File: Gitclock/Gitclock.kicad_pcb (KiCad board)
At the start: 2 copper layers, 140 x 90 mm, 41 parts, among them J1 PJ-102AH, J2 Conn_01x06, SW1 Omron_B3F_SPST, SW5 RotaryEncoder_Switch, U1 ATmega328-PU, U2 L7805, U3 MAX7219, U4 DS1307_DIP-8, Y1 Crystal_16MHz, Y2 Crystal_32768Hz

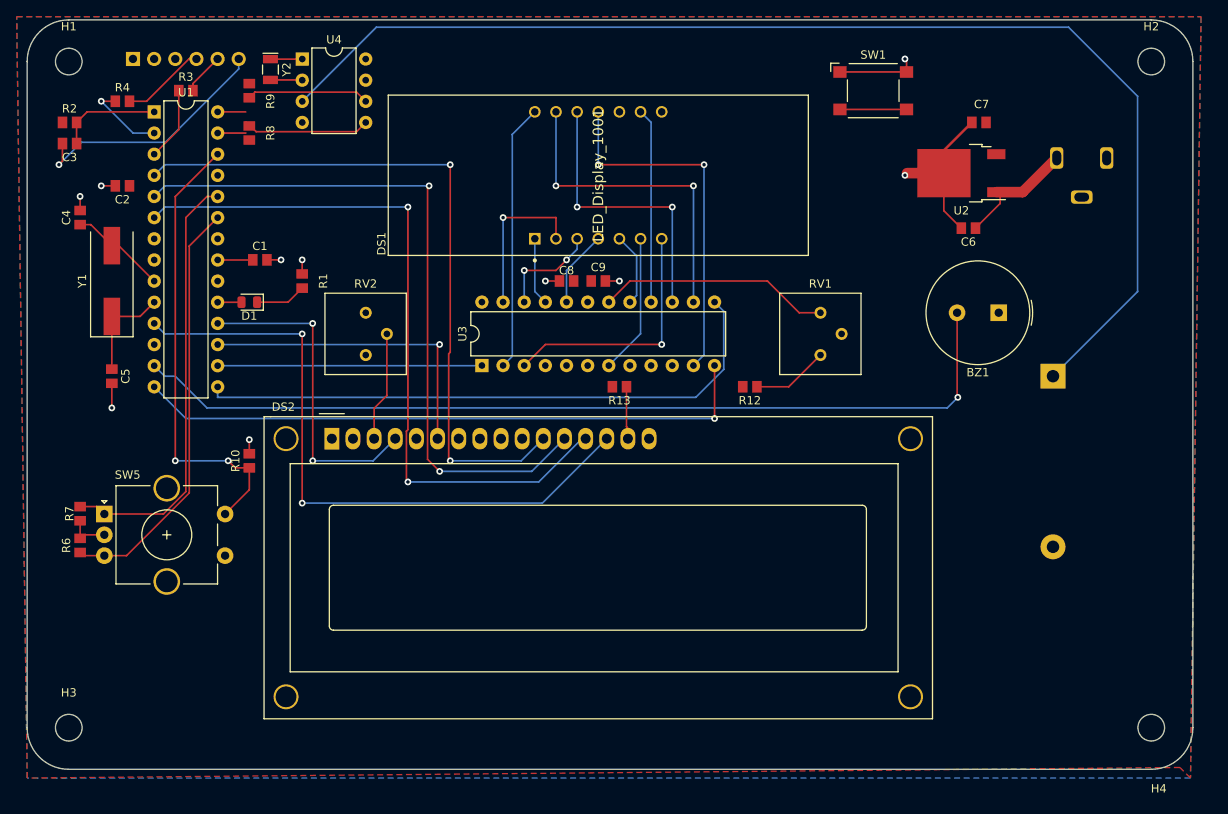
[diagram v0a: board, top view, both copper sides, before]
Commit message: Finished Routing each individual connections
Waiting for approval
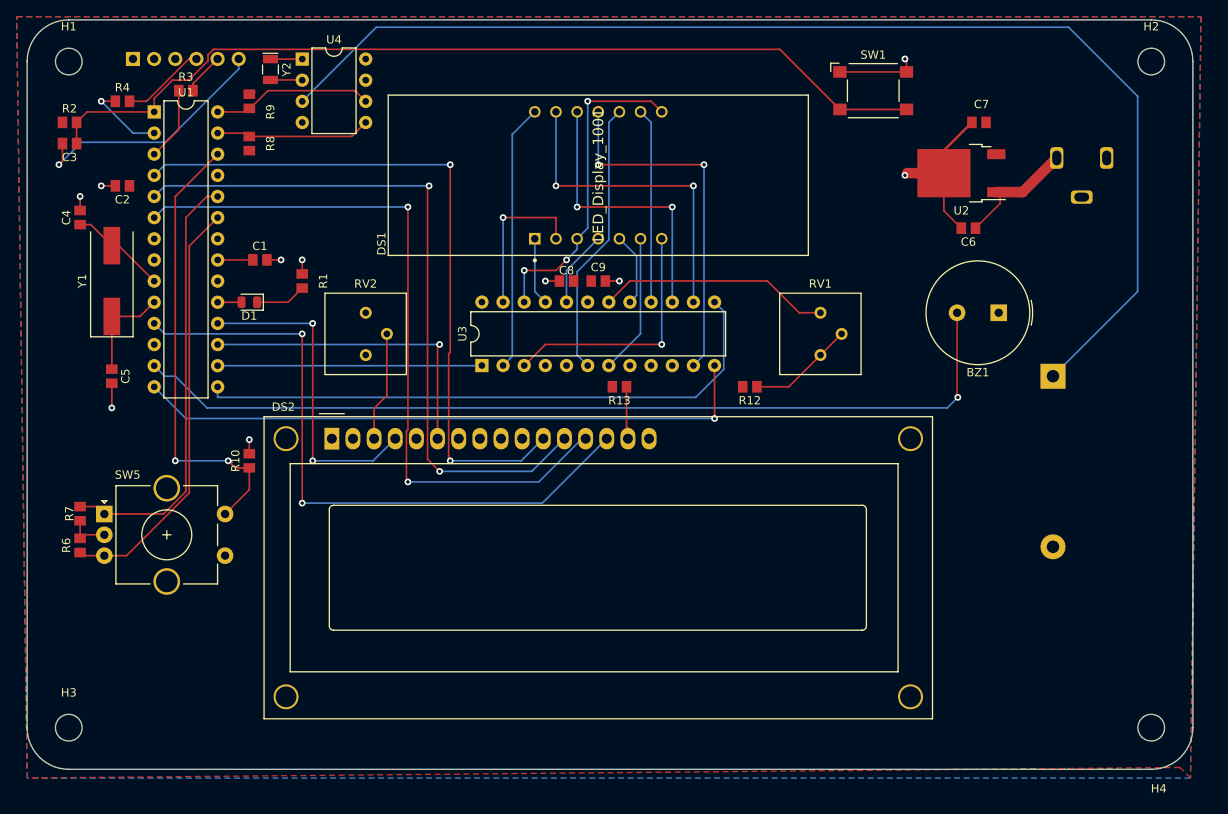
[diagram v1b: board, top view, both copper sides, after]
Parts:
- moved R8 1.27 mm to (106.7, 69.8)
- moved R9 1.27 mm to (106.7, 64.8)
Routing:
- net RESET: track 20.4 -> 110.2 mm
- net Net-(DS1-Pad10): track 0.00 -> 33.1 mm
- net Net-(DS1-Pad3): track 12.5 -> 38.9 mm, vias 2 -> 3
- net Net-(R12-Pad1): track 9.21 -> 12.8 mm
- net VCC: track 1.01 -> 1.96 mm
- net SCL: track 18.7 -> 19.4 mm
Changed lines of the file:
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@@
     (fp_line (start -5 28) (end -5 3) (layer "F.SilkS") (width 0.12))
     (fp_line (start -8.14 33.64) (end 72.14 33.64) (layer "F.SilkS") (width 0.12))
-    (fp_arc (start 64.20104 22.49932) (mid 64.054473 22.853115) (end 63.70066 22.9997) (layer "F.SilkS") (width 0.12))
+    (fp_arc (start 64.20104 22.49932) (mid 64.054479 22.85315) (end 63.70066 22.9997) (layer "F.SilkS") (width 0.12))
     (fp_arc (start -0.29972 8.49884) (mid -0.153162 8.145018) (end 0.20066 7.99846) (layer "F.SilkS") (width 0.12))
     (fp_arc (start 0.20066 22.9997) (mid -0.153162 22.853142) (end -0.29972 22.49932) (layer "F.SilkS") (width 0.12))
@@
   )
   (footprint "footprints:R_0805_2012Metric" (layer "F.Cu")
-    (at 106.68 63.5 -90)
+    (at 106.68 64.77 -90)
     (descr "Resistor SMD 0805 (2012 Metric), square (rectangular) end terminal, IPC_7351 nominal, (Body size source: http://www.tortai-tech.com/upload/download/2011102023233369053.pdf), generated with kicad-footprint-generator")
     (tags "resistor")
@@
   )
   (footprint "footprints:R_0805_2012Metric" (layer "F.Cu")
-    (at 106.68 68.58 90)
+    (at 106.68 69.85 90)
     (descr "Resistor SMD 0805 (2012 Metric), square (rectangular) end terminal, IPC_7351 nominal, (Body size source: http://www.tortai-tech.com/upload/download/2011102023233369053.pdf), generated with kicad-footprint-generator")
     (tags "resistor")
@@
   (segment (start 107.09 83.83) (end 107.1 83.82) (width 0.2032) (layer "F.Cu") (net 2))
   (segment (start 102.88 83.83) (end 107.09 83.83) (width 0.2032) (layer "F.Cu") (net 2))
+  (segment (start 97.456501 62.23) (end 95.26 64.426501) (width 0.2032) (layer "F.Cu") (net 3))
+  (segment (start 101.715689 59.936754) (end 99.422443 62.23) (width 0.2032) (layer "F.Cu") (net 3))
+  (segment (start 101.715689 59.211868) (end 101.715689 59.936754) (width 0.2032) (layer "F.Cu") (net 3))
+  (segment (start 99.422443 62.23) (end 97.456501 62.23) (width 0.2032) (layer "F.Cu") (net 3))
   (segment (start 87.2 66.05) (end 95.26 66.05) (width 0.2032) (layer "F.Cu") (net 3))
+  (segment (start 177.61 65.75) (end 170.395689 58.535689) (width 0.2032) (layer "F.Cu") (net 3))
   (segment (start 85.94 67.31) (end 87.2 66.05) (width 0.2032) (layer "F.Cu") (net 3))
   (segment (start 85.94 67.31) (end 85.94 69.85) (width 0.2032) (layer "F.Cu") (net 3))
+  (segment (start 102.391868 58.535689) (end 101.715689 59.211868) (width 0.2032) (layer "F.Cu") (net 3))
+  (segment (start 95.26 64.426501) (end 95.26 66.05) (width 0.2032) (layer "F.Cu") (net 3))
+  (segment (start 170.395689 58.535689) (end 102.391868 58.535689) (width 0.2032) (layer "F.Cu") (net 3))
   (segment (start 177.61 65.75) (end 185.61 65.75) (width 0.2032) (layer "F.Cu") (net 3))
   (segment (start 84.24 71.97) (end 83.82 72.39) (width 0.2032) (layer "F.Cu") (net 4))
@@
   (segment (start 143.51 85.09) (end 144.78 83.82) (width 0.2032) (layer "F.Cu") (net 12))
   (segment (start 139.7 85.09) (end 143.51 85.09) (width 0.2032) (layer "F.Cu") (net 12))
+  (segment (start 147.32 64.77) (end 154.94 64.77) (width 0.2032) (layer "F.Cu") (net 12))
+  (segment (start 154.94 64.77) (end 156.21 66.04) (width 0.2032) (layer "F.Cu") (net 12))
   (via (at 139.7 85.09) (size 0.8128) (drill 0.4064) (layers "F.Cu" "B.Cu") (net 12))
+  (via (at 147.32 64.77) (size 0.8128) (drill 0.4064) (layers "F.Cu" "B.Cu") (net 12))
   (via (at 144.78 83.82) (size 0.8128) (drill 0.4064) (layers "F.Cu" "B.Cu") (net 12))
+  (segment (start 146.05 81.28) (end 147.32 80.01) (width 0.2032) (layer "B.Cu") (net 12))
   (segment (start 139.695 85.095) (end 139.7 85.09) (width 0.2032) (layer "B.Cu") (net 12))
+  (segment (start 147.32 80.01) (end 147.32 64.77) (width 0.2032) (layer "B.Cu") (net 12))
   (segment (start 144.78 83.82) (end 146.05 82.55) (width 0.2032) (layer "B.Cu") (net 12))
   (segment (start 146.05 82.55) (end 146.05 81.28) (width 0.2032) (layer "B.Cu") (net 12))
@@
   (segment (start 154.934996 88.889992) (end 154.934996 67.304996) (width 0.2032) (layer "B.Cu") (net 18))
   (segment (start 154.934996 67.304996) (end 153.67 66.04) (width 0.2032) (layer "B.Cu") (net 18))
+  (segment (start 149.86 81.430311) (end 149.86 67.31) (width 0.2032) (layer "B.Cu") (net 19))
+  (segment (start 147.315 96.51) (end 146.05 95.245) (width 0.2032) (layer "B.Cu") (net 19))
+  (segment (start 149.86 67.31) (end 151.13 66.04) (width 0.2032) (layer "B.Cu") (net 19))
+  (segment (start 146.05 85.240311) (end 149.86 81.430311) (width 0.2032) (layer "B.Cu") (net 19))
+  (segment (start 146.05 95.245) (end 146.05 85.240311) (width 0.2032) (layer "B.Cu") (net 19))
   (segment (start 161.29 72.39) (end 148.59 72.39) (width 0.2032) (layer "F.Cu") (net 20))
   (via (at 148.59 72.39) (size 0.8128) (drill 0.4064) (layers "F.Cu" "B.Cu") (net 20))
@@
   (segment (start 150.28 99.06) (end 149.86 99.06) (width 0.2032) (layer "F.Cu") (net 34))
   (segment (start 146.9 88.475) (end 147.315 88.89) (width 0.2032) (layer "F.Cu") (net 34))
+  (segment (start 106.68 64.35) (end 107.354311 63.675689) (width 0.2032) (layer "F.Cu") (net 34))
   (segment (start 99.06 78.74) (end 101.59 76.21) (width 0.2032) (layer "F.Cu") (net 35))
   (segment (start 86.36 113.45) (end 88.38 113.45) (width 0.2032) (layer "F.Cu") (net 35))
@@
   (segment (start 97.79 107.95) (end 104.14 107.95) (width 0.2032) (layer "B.Cu") (net 36))
   (segment (start 171.465 99.06) (end 175.275 95.25) (width 0.2032) (layer "F.Cu") (net 37))
+  (segment (start 175.275 95.25) (end 177.815 92.71) (width 0.2032) (layer "F.Cu") (net 37))
   (segment (start 167.64 99.06) (end 171.465 99.06) (width 0.2032) (layer "F.Cu") (net 37))
   (segment (start 162.555 102.865) (end 162.555 96.51) (width 0.2032) (layer "F.Cu") (net 38))
@@
   (segment (start 163.659311 89.994311) (end 163.659311 96.967422) (width 0.2032) (layer "B.Cu") (net 45))
   (segment (start 160.296733 100.33) (end 102.87 100.33) (width 0.2032) (layer "B.Cu") (net 45))
-  (segment (start 106.27 67.32) (end 106.68 67.73) (width 0.2032) (layer "F.Cu") (net 46))
-  (segment (start 119.555689 68.424311) (end 120.66 67.32) (width 0.2032) (layer "F.Cu") (net 46))
+  (segment (start 106.68 69) (end 118.98 69) (width 0.2032) (layer "F.Cu") (net 46))
+  (segment (start 106.27 68.59) (end 106.68 69) (width 0.2032) (layer "F.Cu") (net 46))
   (segment (start 102.88 68.59) (end 106.27 68.59) (width 0.2032) (layer "F.Cu") (net 46))
-  (segment (start 107.499311 68.424311) (end 119.555689 68.424311) (width 0.2032) (layer "F.Cu") (net 46))
-  (segment (start 106.68 67.73) (end 106.805 67.73) (width 0.2032) (layer "F.Cu") (net 46))
-  (segment (start 106.805 67.73) (end 107.499311 68.424311) (width 0.2032) (layer "F.Cu") (net 46))
-  (segment (start 107.354311 63.675689) (end 119.555689 63.675689) (width 0.2032) (layer "F.Cu") (net 47))
-  (segment (start 106.25 64.78) (end 106.68 64.35) (width 0.2032) (layer "F.Cu") (net 47))
+  (segment (start 118.98 69) (end 120.66 67.32) (width 0.2032) (layer "F.Cu") (net 46))
+  (segment (start 106.25 66.05) (end 106.68 65.62) (width 0.2032) (layer "F.Cu") (net 47))
+  (segment (start 119.38 63.5) (end 120.66 64.78) (width 0.2032) (layer "F.Cu") (net 47))
+  (segment (start 106.68 65.62) (end 106.805 65.62) (width 0.2032) (layer "F.Cu") (net 47))
   (segment (start 102.88 66.05) (end 106.25 66.05) (width 0.2032) (layer "F.Cu") (net 47))
-  (segment (start 119.555689 63.675689) (end 120.66 64.78) (width 0.2032) (layer "F.Cu") (net 47))
-  (segment (start 106.68 64.35) (end 107.354311 63.675689) (width 0.2032) (layer "F.Cu") (net 47))
+  (segment (start 108.925 63.5) (end 119.38 63.5) (width 0.2032) (layer "F.Cu") (net 47))
+  (segment (start 106.805 65.62) (end 108.925 63.5) (width 0.2032) (layer "F.Cu") (net 47))
   (segment (start 134.595 96.53) (end 134.615 96.51) (width 0.2032) (layer "B.Cu") (net 48))
   (segment (start 102.88 96.53) (end 134.595 96.53) (width 0.2032) (layer "B.Cu") (net 48))

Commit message: Test Points Added to Clock
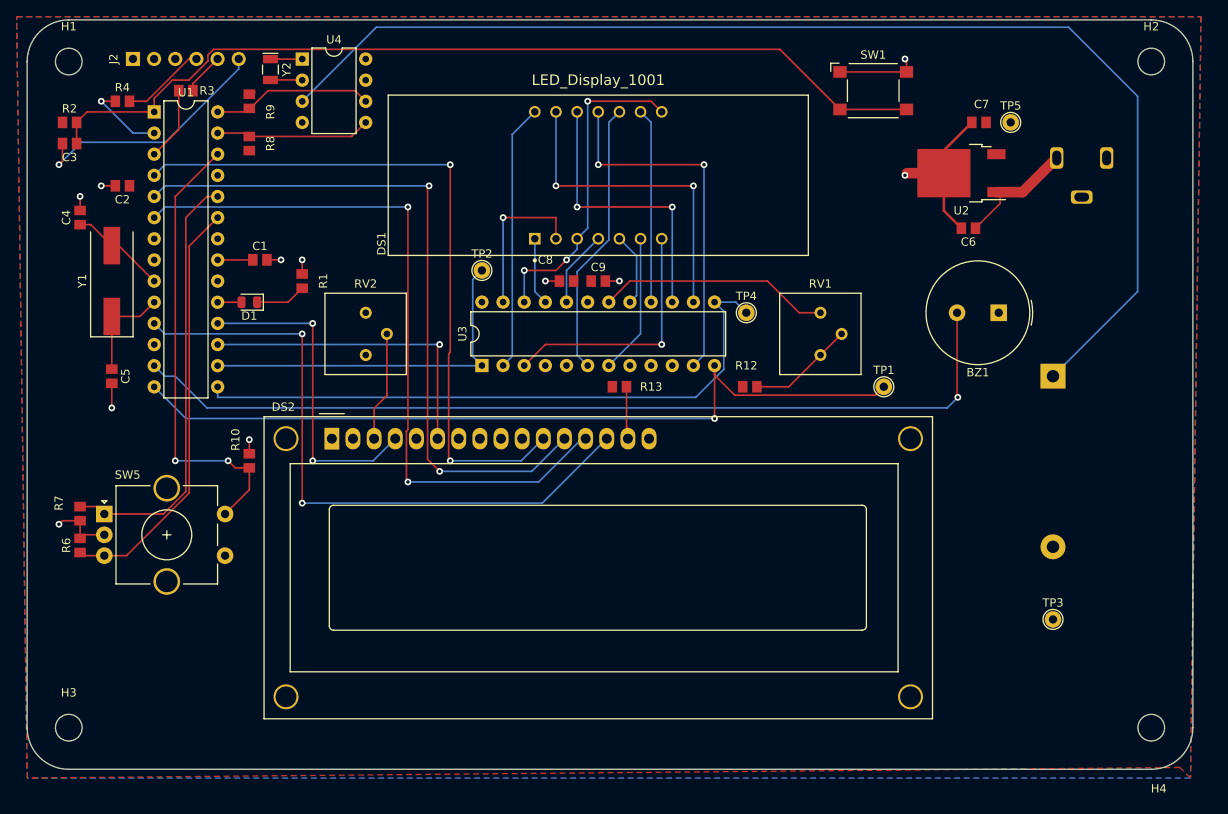
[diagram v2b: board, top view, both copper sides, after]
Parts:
- added TP1: TestPoint, footprints:TestPoint_THTPad_D2.0mm_Drill1.0mm, F.Cu at (182.9, 99.1)
- added TP2: TestPoint, footprints:TestPoint_THTPad_D2.0mm_Drill1.0mm, F.Cu at (134.6, 85.1)
- added TP3: TestPoint, footprints:TestPoint_THTPad_D2.0mm_Drill1.0mm, F.Cu at (203.2, 127.0)
- added TP4: TestPoint, footprints:TestPoint_THTPad_D2.0mm_Drill1.0mm, F.Cu at (166.4, 90.2)
- added TP5: TestPoint, footprints:TestPoint_THTPad_D2.0mm_Drill1.0mm, F.Cu at (198.1, 67.3)
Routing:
- net LOAD: track 75.2 -> 98.1 mm
- net DATA: track 31.7 -> 44.1 mm
- net CLK: track 72.0 -> 76.3 mm
- net GND: track 49.5 -> 52.2 mm, vias 10 -> 11

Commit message: clock_complete
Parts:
- added J3: Conn_02x03_Odd_Even, footprints:PinHeader_2x03_P2.54mm_Vertical, F.Cu at (99.1, 130.8)
- moved R1 3.59 mm to (110.5, 88.9), turned to 0 degrees
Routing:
- net RESET: track 110.2 -> 176.8 mm
- net LED_SCK: track 2.87 -> 51.4 mm
- net MOSI: track 38.1 -> 81.0 mm
- net RS: track 38.9 -> 68.1 mm
- net Net-(D1-Pad1): track 6.11 -> 2.02 mm
- net Net-(DS1-Pad12): track 34.3 -> 36.1 mm
- net VCC: track 1.96 -> 0.95 mm
- net GND: track 52.2 -> 51.7 mm

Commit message: CuckcooTicTocFINALCLOCK
Last Upload onto Github
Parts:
- removed RV1: R_POT_10K, footprints:Potentiometer_Bourns_3386P_Vertical
- added Q1: NPN_2N3904_SOT23, footprints:SOT-23, F.Cu at (182.9, 86.4)
- added R11: R_0805_2.2K, footprints:R_0805_2012Metric, F.Cu at (92.7, 105.4)
- added R5: R_0805_1K, footprints:R_0805_2012Metric, F.Cu at (203.2, 90.2)
- C9: value C_0805_0.1uf -> C_0805_10uf
- J1: value PJ-102AH -> VAL**
- R12: value R_0805_10K -> R_0805_22K
- moved R12 13.2 mm to (176.5, 90.2)
- moved D1 3.81 mm to (110.5, 88.9)
- moved R1 3.81 mm to (106.7, 88.9)
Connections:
- BZ1 pad 1: GND -> VCC
- BZ1 pad 2: BUZZER -> Net-(BZ1-Pad2)
- D1 pad 1: Net-(D1-Pad1) -> GND
- D1 pad 2: LED_SCK -> Net-(R1-Pad2)
- R1 pad 1: Net-(D1-Pad1) -> LED_SCK
- R1 pad 2: GND -> Net-(R1-Pad2)
- R12 pad 1: Net-(R12-Pad1) -> VCC
- R12 pad 2: VCC -> Net-(U3-Pad18)
- U1 pad 25: Select_B -> unconnected-(U1-Pad25)
- U3 pad 18: Net-(RV1-Pad3) -> Net-(U3-Pad18)
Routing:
- net BUZZER: track 109.3 -> 9.08 mm, vias 1 -> 0
- net Net-(Q1-Pad1): track 0.00 -> 98.9 mm, vias 0 -> 4
- net Net-(U3-Pad18): track 0.00 -> 28.0 mm
- net Net-(RV1-Pad3): track 28.0 -> 0.00 mm
- net Net-(BZ1-Pad2): track 0.00 -> 21.6 mm
- net Net-(R12-Pad1): track 12.8 -> 0.00 mm
- net GND: track 51.7 -> 57.2 mm, vias 11 -> 13
- net Net-(R1-Pad2): track 0.00 -> 2.02 mm
- net Net-(D1-Pad1): track 2.02 -> 0.00 mm
- net VCC: track 0.95 -> 0.00 mm
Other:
- board text added: "Cuckoo Tic Toc"

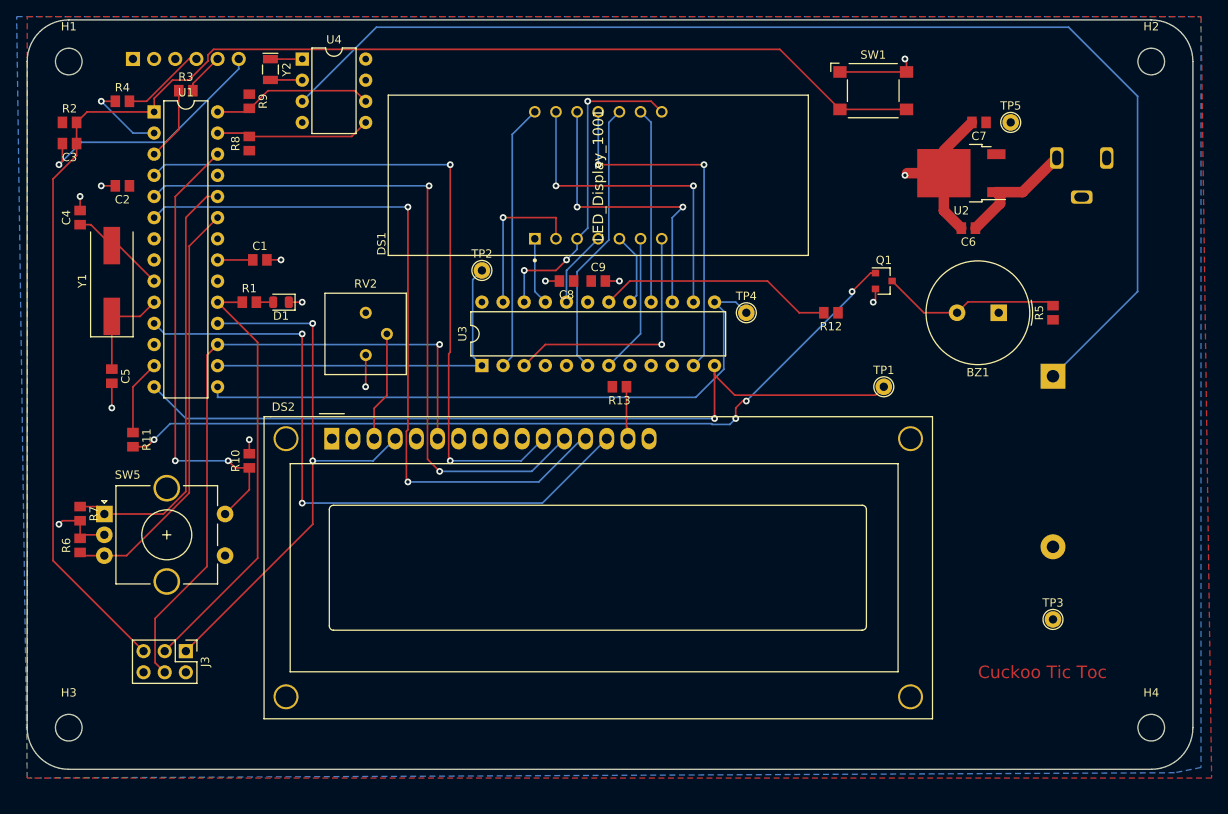
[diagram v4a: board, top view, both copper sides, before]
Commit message: changed pull down to pull up and swapped RX and TX connection
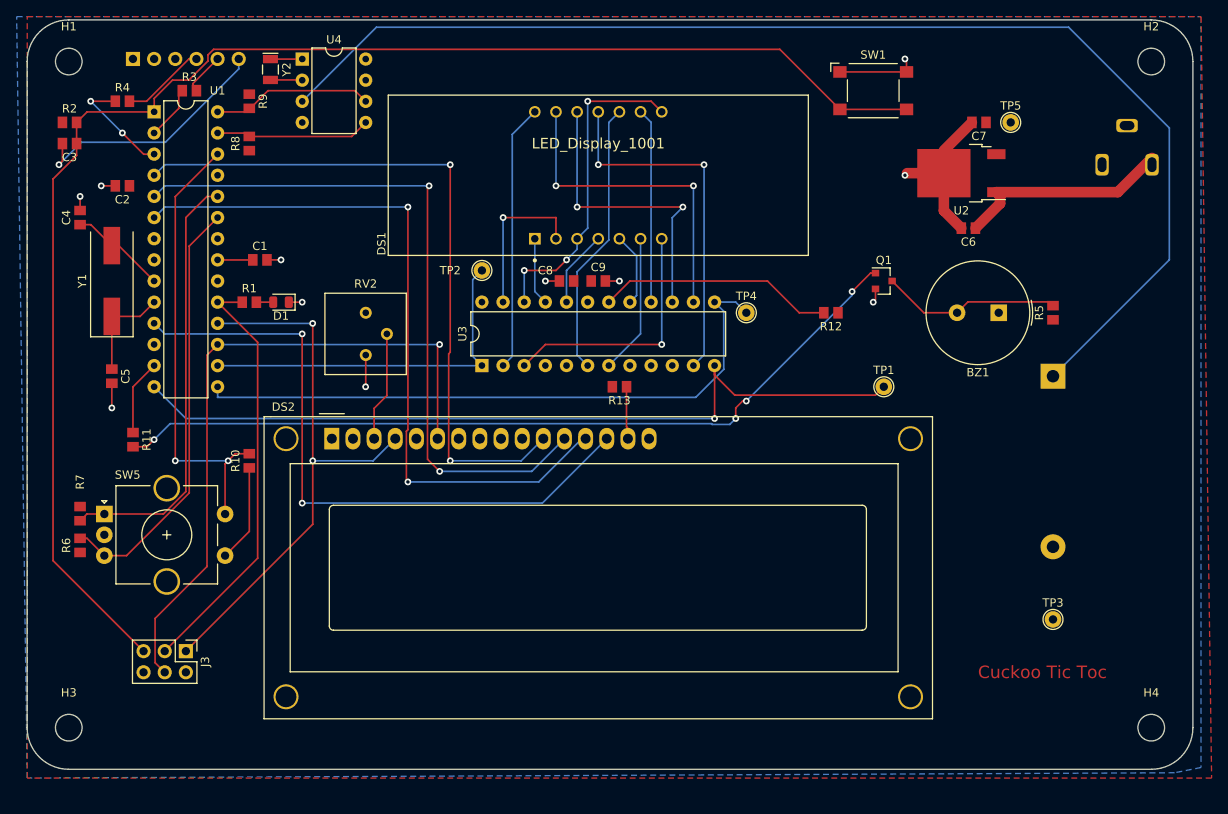
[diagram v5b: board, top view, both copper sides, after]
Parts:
- J1: value VAL** -> PJ-102AH
- moved J1 5.50 mm to (212.1, 72.4), turned to -90 degrees
- moved R3 0.42 mm to (99.5, 63.5)
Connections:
- R10 pad 1: MENU_B -> VCC
- R10 pad 2: GND -> MENU_B
- R3 pad 1: TXD -> RXD
- R4 pad 1: RXD -> TXD
- R6 pad 1: MENU SCROLL -> VCC
- R6 pad 2: GND -> MENU SCROLL
- R7 pad 1: MENU OUTPUT2 -> VCC
- R7 pad 2: GND -> MENU OUTPUT2
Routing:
- net VCC: track 0.00 -> 11.7 mm
- net Net-(C6-Pad1): track 14.7 -> 26.1 mm
- net GND: track 57.2 -> 48.0 mm, vias 13 -> 11
- net TXD: track 8.85 -> 13.2 mm, vias 0 -> 2
- net RXD: track 9.63 -> 6.32 mm, vias 1 -> 0
- net +BATT: track 145.3 -> 148.4 mm
- net MENU SCROLL: track 50.9 -> 51.6 mm
